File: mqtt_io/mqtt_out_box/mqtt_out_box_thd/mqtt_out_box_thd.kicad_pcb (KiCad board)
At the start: 2 copper layers, 124.5 x 133.1 mm, 63 parts, among them J1 Conn_01x02, J3 Conn_01x04_Pin, K1 FINDER-40.52, K2 FINDER-40.52, K3 FINDER-40.52, K4 FINDER-40.52, K5 FINDER-40.52, K6 FINDER-40.52, K7 FINDER-40.52, K8 FINDER-40.52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

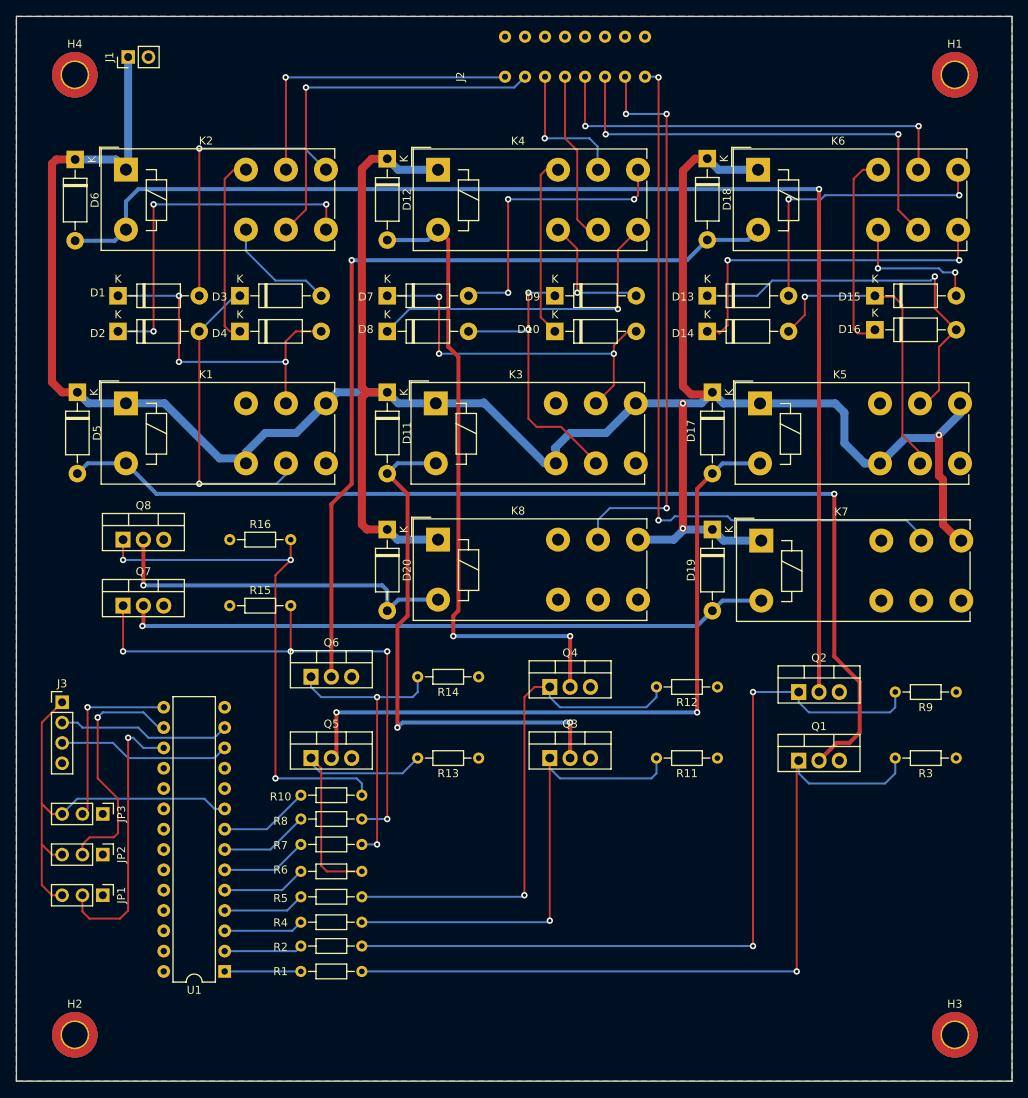
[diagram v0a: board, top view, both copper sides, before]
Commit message: Pullup für ic2 eingefügt (4k7)
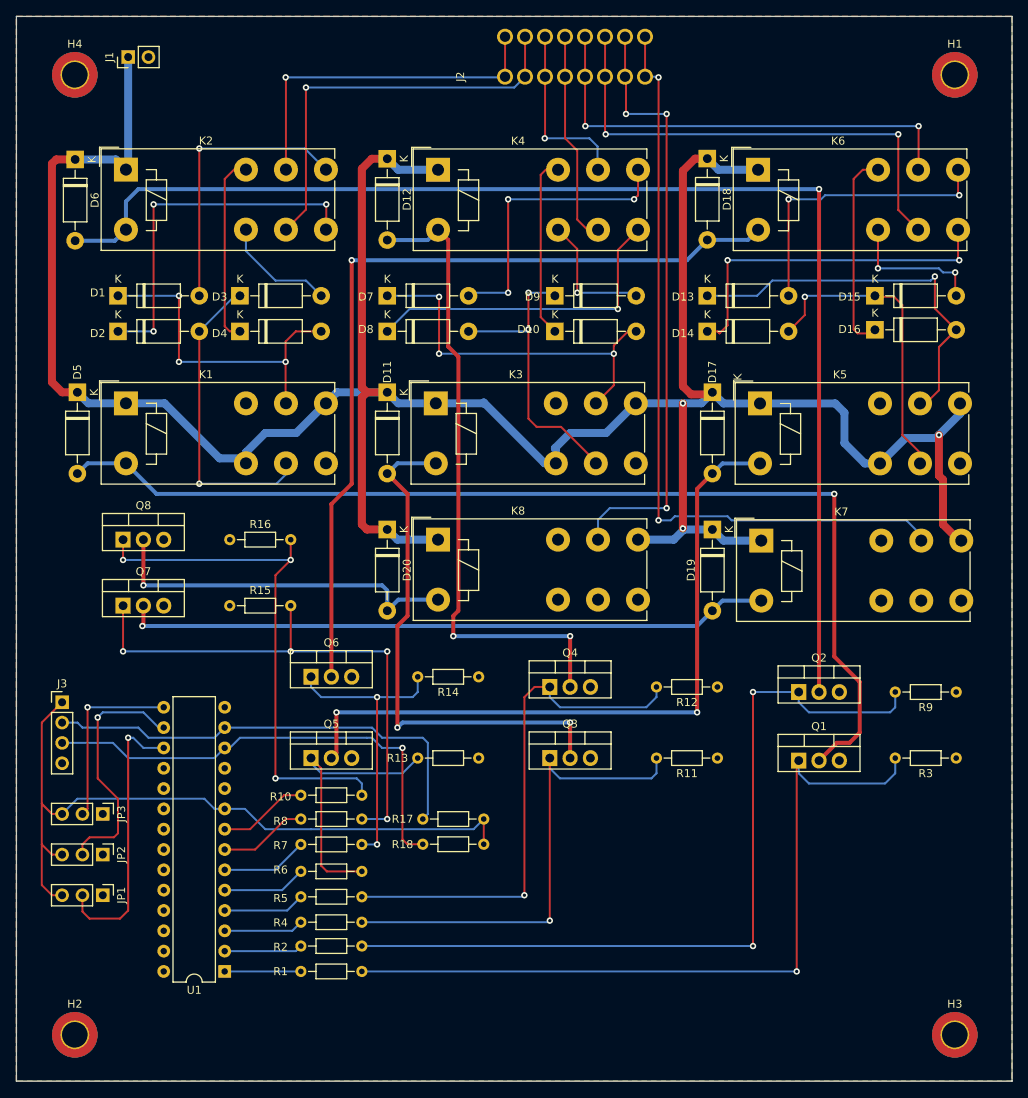
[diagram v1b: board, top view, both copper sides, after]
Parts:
- added R17: 4k7, Resistor_THT:R_Axial_DIN0204_L3.6mm_D1.6mm_P7.62mm_Horizontal, F.Cu at (63.5, 113.0)
- added R18: 4k7, Resistor_THT:R_Axial_DIN0204_L3.6mm_D1.6mm_P7.62mm_Horizontal, F.Cu at (63.5, 116.2)
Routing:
- net Net-(J3-Pin_3): track 21.6 -> 59.2 mm, vias 0 -> 1
- net VCC: track 54.7 -> 91.8 mm
- net Net-(J3-Pin_2): track 21.6 -> 57.6 mm
- net Pin8: track 70.7 -> 75.7 mm
- net Pin7: track 91.8 -> 96.8 mm
- net Net-(J2-io-Pad6): track 56.8 -> 61.8 mm
- net Net-(J2-io-Pad5): track 53.3 -> 58.3 mm
- net Net-(J2-io-Pad4): track 21.6 -> 26.6 mm
- net Net-(J2-io-Pad2): track 46.7 -> 51.7 mm
- net Net-(J2-io-Pad1): track 39.0 -> 44.0 mm
- net Net-(J2-io-Pad3): track 17.7 -> 22.7 mm

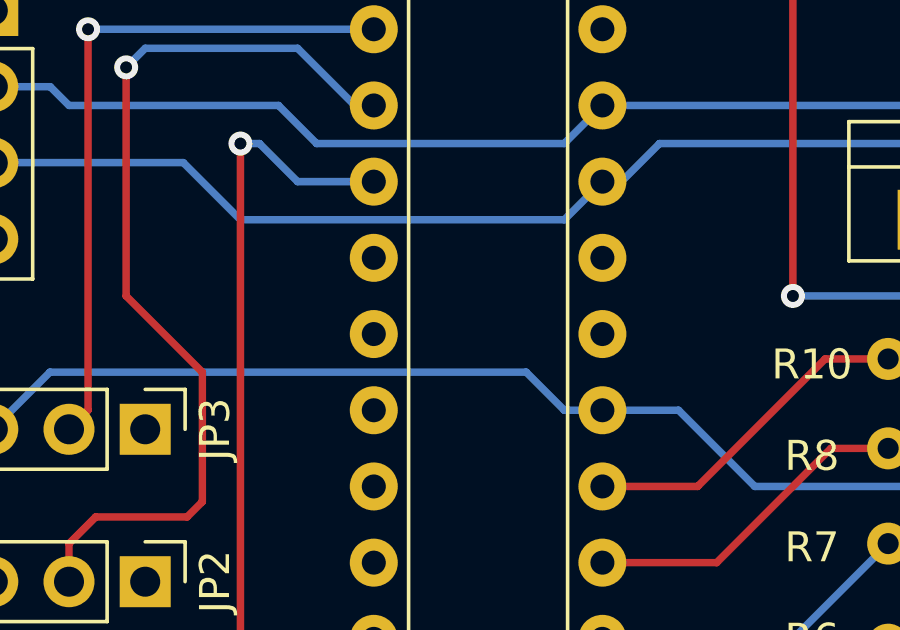
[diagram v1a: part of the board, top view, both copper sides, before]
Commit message: neue Dateien eingefügt.
out Platine rev 2, testprogramm für pi pico
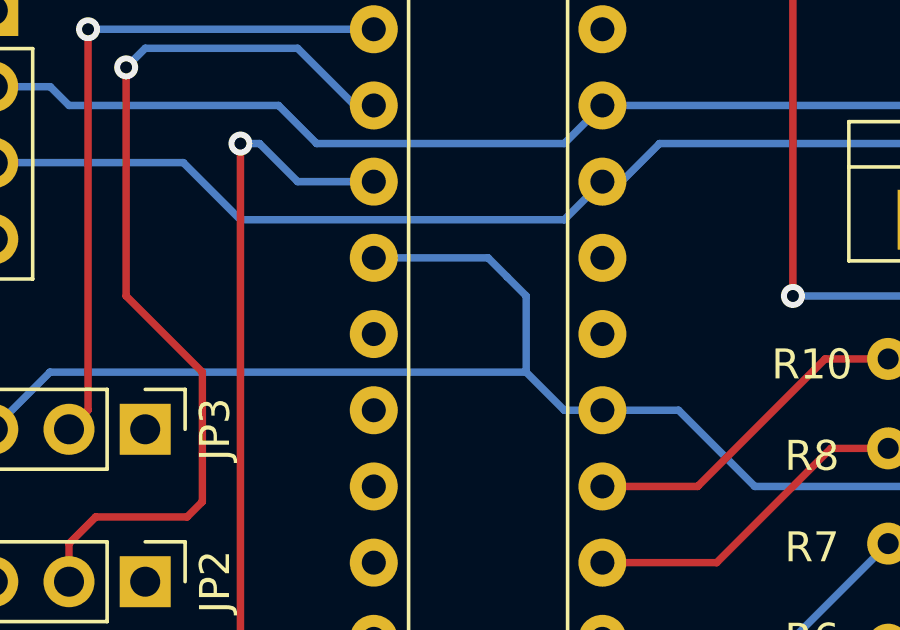
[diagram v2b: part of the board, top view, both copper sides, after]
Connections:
- U1 pad 18: GND -> VCC
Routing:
- net VCC: track 91.8 -> 100.0 mm
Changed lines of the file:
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@@
       (net 30 "Net-(JP1-C)") (pinfunction "A2") (pintype "input"))
     (pad "18" thru_hole oval (at 7.62 25.4 180) (size 1.6 1.6) (drill 0.8) (layers "*.Cu" "*.Mask")
-      (net 20 "GND") (pinfunction "~{RESET}") (pintype "input"))
+      (net 27 "VCC") (pinfunction "~{RESET}") (pintype "input"))
     (pad "19" thru_hole oval (at 7.62 22.86 180) (size 1.6 1.6) (drill 0.8) (layers "*.Cu" "*.Mask")
       (net 59 "unconnected-(U1-INTB-Pad19)") (pinfunction "INTB") (pintype "tri_state"))
@@
   (segment (start 37.465 111.76) (end 38.735 111.76) (width 0.25) (layer "B.Cu") (net 27))
   (segment (start 20.32 110.49) (end 36.195 110.49) (width 0.25) (layer "B.Cu") (net 27))
+  (segment (start 31.115 106.68) (end 34.925 106.68) (width 0.25) (layer "B.Cu") (net 27))
   (segment (start 18.415 112.395) (end 20.32 110.49) (width 0.25) (layer "B.Cu") (net 27))
+  (segment (start 34.925 106.68) (end 35.56 107.315) (width 0.25) (layer "B.Cu") (net 27))
+  (segment (start 36.195 107.95) (end 36.195 110.49) (width 0.25) (layer "B.Cu") (net 27))
+  (segment (start 35.56 107.315) (end 36.195 107.95) (width 0.25) (layer "B.Cu") (net 27))
   (segment (start 69.85 114.3) (end 71.12 113.03) (width 0.25) (layer "B.Cu") (net 27))
   (segment (start 36.195 110.49) (end 37.465 111.76) (width 0.25) (layer "B.Cu") (net 27))
